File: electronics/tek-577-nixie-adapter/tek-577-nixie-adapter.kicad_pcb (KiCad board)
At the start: 2 copper layers, 31.7 x 61 mm, 3 parts, among them J1 C, J2 B, J3 E

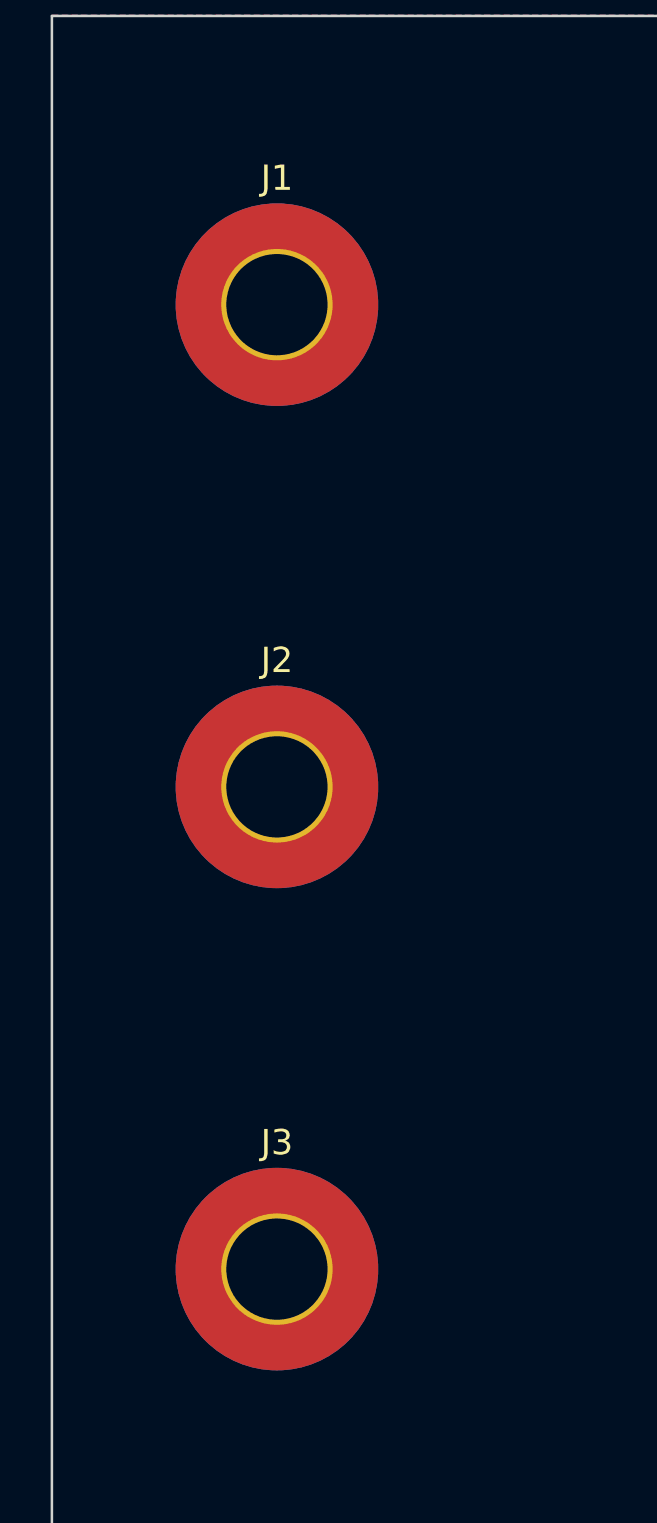
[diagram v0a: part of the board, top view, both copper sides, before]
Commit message: adding symbols
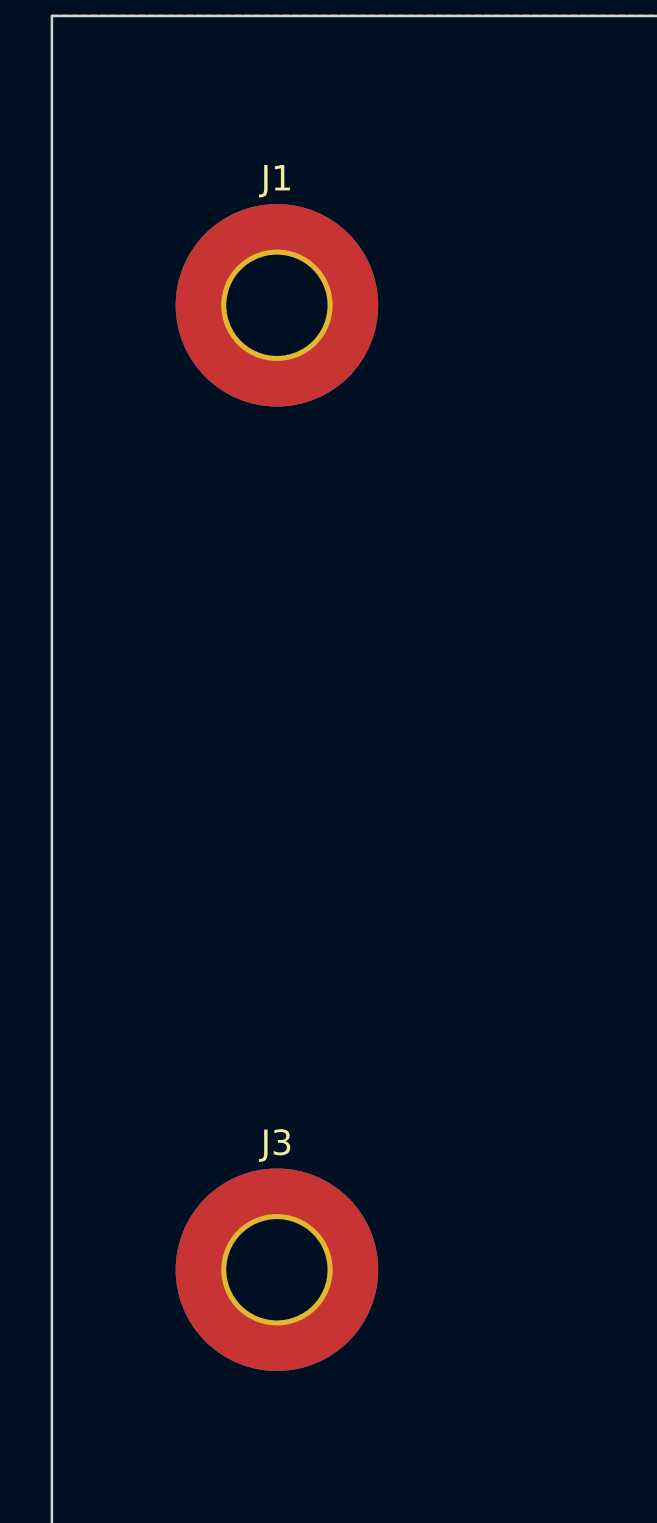
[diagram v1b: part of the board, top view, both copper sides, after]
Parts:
- removed J2: B, MountingHole:MountingHole_4mm_Pad_TopBottom
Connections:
- J1 pad 1: (no net) -> /C
- J3 pad 1: (no net) -> /E
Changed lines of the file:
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@@
   )
   (net 0 "")
+  (net 1 "/C")
+  (net 2 "/E")
   (footprint "MountingHole:MountingHole_4mm_Pad_TopBottom" (layer "F.Cu")
-    (at 134.62 113.005)
+    (at 134.62 74.93)
     (descr "Mounting Hole 4mm")
     (tags "mounting hole 4mm")
-    (property "Sheetfile" "tek-577-fixture-proto.kicad_sch")
+    (property "Sheetfile" "tek-577-nixie-adapter.kicad_sch")
+    (property "Sheetname" "")
+    (property "ki_description" "Generic connector, single row, 01x01, script generated")
+    (property "ki_keywords" "connector")
+    (attr exclude_from_pos_files)
+    (fp_text reference "J1" (at 0 -5) (layer "F.SilkS")
+        (effects (font (size 1 1) (thickness 0.15)))
+    )
+    (fp_text value "C" (at 0 5) (layer "F.Fab")
+        (effects (font (size 1 1) (thickness 0.15)))
+    )
+    (fp_text user "${REFERENCE}" (at 0 0) (layer "F.Fab")
+        (effects (font (size 1 1) (thickness 0.15)))
+    )
+    (fp_circle (center 0 0) (end 4 0)
+      (stroke (width 0.15) (type solid)) (fill none) (layer "Cmts.User"))
+    (fp_circle (center 0 0) (end 4.25 0)
+      (stroke (width 0.05) (type solid)) (fill none) (layer "F.CrtYd"))
+    (pad "1" thru_hole circle (at 0 0) (size 4.4 4.4) (drill 4) (layers "*.Cu" "*.Mask")
+      (net 1 "/C") (pinfunction "Pin_1") (pintype "passive"))
+    (pad "1" connect circle (at 0 0) (size 8 8) (layers "F.Cu" "F.Mask")
+      (net 1 "/C") (pinfunction "Pin_1") (pintype "passive"))
+    (pad "1" connect circle (at 0 0) (size 8 8) (layers "B.Cu" "B.Mask")
+      (net 1 "/C") (pinfunction "Pin_1") (pintype "passive"))
+  )
+  (footprint "MountingHole:MountingHole_4mm_Pad_TopBottom" (layer "F.Cu")
+    (at 134.62 113.03)
+    (descr "Mounting Hole 4mm")
+    (tags "mounting hole 4mm")
+    (property "Sheetfile" "tek-577-nixie-adapter.kicad_sch")
     (property "Sheetname" "")
     (property "ki_description" "Generic connector, single row, 01x01, script generated")
@@
       (stroke (width 0.05) (type solid)) (fill none) (layer "F.CrtYd"))
     (pad "1" thru_hole circle (at 0 0) (size 4.4 4.4) (drill 4) (layers "*.Cu" "*.Mask")
-      (pinfunction "Pin_1") (pintype "passive"))
+      (net 2 "/E") (pinfunction "Pin_1") (pintype "passive"))
     (pad "1" connect circle (at 0 0) (size 8 8) (layers "F.Cu" "F.Mask")
-      (pinfunction "Pin_1") (pintype "passive"))
+      (net 2 "/E") (pinfunction "Pin_1") (pintype "passive"))
     (pad "1" connect circle (at 0 0) (size 8 8) (layers "B.Cu" "B.Mask")
-      (pinfunction "Pin_1") (pintype "passive"))
-  )
-  (footprint "MountingHole:MountingHole_4mm_Pad_TopBottom" (layer "F.Cu")
-    (at 134.62 93.955)
-    (descr "Mounting Hole 4mm")
-    (tags "mounting hole 4mm")
-    (property "Sheetfile" "tek-577-fixture-proto.kicad_sch")
-    (property "Sheetname" "")
-    (property "ki_description" "Generic connector, single row, 01x01, script generated")
-    (property "ki_keywords" "connector")
-    (attr exclude_from_pos_files)
-    (fp_text reference "J2" (at 0 -5) (layer "F.SilkS")
-        (effects (font (size 1 1) (thickness 0.15)))
-    )
-    (fp_text value "B" (at 0 5) (layer "F.Fab")
-        (effects (font (size 1 1) (thickness 0.15)))
-    )
-    (fp_text user "${REFERENCE}" (at 0 0) (layer "F.Fab")
-        (effects (font (size 1 1) (thickness 0.15)))
-    )
-    (fp_circle (center 0 0) (end 4 0)
-      (stroke (width 0.15) (type solid)) (fill none) (layer "Cmts.User"))
-    (fp_circle (center 0 0) (end 4.25 0)
-      (stroke (width 0.05) (type solid)) (fill none) (layer "F.CrtYd"))
-    (pad "1" thru_hole circle (at 0 0) (size 4.4 4.4) (drill 4) (layers "*.Cu" "*.Mask")
-      (pinfunction "Pin_1") (pintype "passive"))
-    (pad "1" connect circle (at 0 0) (size 8 8) (layers "F.Cu" "F.Mask")
-      (pinfunction "Pin_1") (pintype "passive"))
-    (pad "1" connect circle (at 0 0) (size 8 8) (layers "B.Cu" "B.Mask")
-      (pinfunction "Pin_1") (pintype "passive"))
-  )
-  (footprint "MountingHole:MountingHole_4mm_Pad_TopBottom" (layer "F.Cu")
-    (at 134.62 74.905)
-    (descr "Mounting Hole 4mm")
-    (tags "mounting hole 4mm")
-    (property "Sheetfile" "tek-577-fixture-proto.kicad_sch")
-    (property "Sheetname" "")
-    (property "ki_description" "Generic connector, single row, 01x01, script generated")
-    (property "ki_keywords" "connector")
-    (attr exclude_from_pos_files)
-    (fp_text reference "J1" (at 0 -5) (layer "F.SilkS")
-        (effects (font (size 1 1) (thickness 0.15)))
-    )
-    (fp_text value "C" (at 0 5) (layer "F.Fab")
-        (effects (font (size 1 1) (thickness 0.15)))
-    )
-    (fp_text user "${REFERENCE}" (at 0 0) (layer "F.Fab")
-        (effects (font (size 1 1) (thickness 0.15)))
-    )
-    (fp_circle (center 0 0) (end 4 0)
-      (stroke (width 0.15) (type solid)) (fill none) (layer "Cmts.User"))
-    (fp_circle (center 0 0) (end 4.25 0)
-      (stroke (width 0.05) (type solid)) (fill none) (layer "F.CrtYd"))
-    (pad "1" thru_hole circle (at 0 0) (size 4.4 4.4) (drill 4) (layers "*.Cu" "*.Mask")
-      (pinfunction "Pin_1") (pintype "passive"))
-    (pad "1" connect circle (at 0 0) (size 8 8) (layers "F.Cu" "F.Mask")
-      (pinfunction "Pin_1") (pintype "passive"))
-    (pad "1" connect circle (at 0 0) (size 8 8) (layers "B.Cu" "B.Mask")
-      (pinfunction "Pin_1") (pintype "passive"))
+      (net 2 "/E") (pinfunction "Pin_1") (pintype "passive"))
   )
   (gr_rect (start 125.73 63.5) (end 157.48 124.46)

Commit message: working footprints
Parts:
- added N1: IN-4, nixie-us:IN-4-DSUB, F.Cu at (145.1, 94.0)
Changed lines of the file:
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@@
   (net 1 "/C")
   (net 2 "/E")
+  (net 3 "unconnected-(N1-Pad1)")
+  (net 4 "unconnected-(N1-Pad5)")
+  (net 5 "unconnected-(N1-Pad3)")
+  (net 6 "unconnected-(N1-Pad2)")
+  (net 7 "unconnected-(N1-Pad0)")
+  (net 8 "unconnected-(N1-Pad7)")
+  (net 9 "unconnected-(N1-Pad9)")
+  (net 10 "unconnected-(N1-Pad4)")
+  (net 11 "unconnected-(N1-Pad6)")
+  (net 12 "unconnected-(N1-Pad8)")
+  (net 13 "unconnected-(N1-A-PadA3)")
   (footprint "MountingHole:MountingHole_4mm_Pad_TopBottom" (layer "F.Cu")
     (at 134.62 74.93)
@@
       (net 1 "/C") (pinfunction "Pin_1") (pintype "passive"))
   )
+  (footprint "nixie-us:IN-4-DSUB" (layer "F.Cu")
+    (at 145.066716 93.968457)
+    (descr "May be used with socket: <b>PL31-P</b>")
+    (property "Sheetfile" "tek-577-nixie-adapter.kicad_sch")
+    (property "Sheetname" "")
+    (fp_text reference "N1" (at 16.51 0) (layer "F.SilkS")
+        (effects (font (size 1.63576 1.63576) (thickness 0.14224)) (justify left bottom))
+    )
+    (fp_text value "IN-4" (at 0 12.7) (layer "F.SilkS")
+        (effects (font (size 1.63576 1.63576) (thickness 0.14224)))
+    )
+    (fp_text user "TOP" (at 0 -12.7) (layer "F.SilkS")
+        (effects (font (size 1.63576 1.63576) (thickness 0.14224)))
+    )
+    (fp_circle (center -0.033137 0.0873) (end 15.785363 0.0873)
+      (stroke (width 0.254) (type solid)) (fill none) (layer "F.SilkS"))
+    (fp_circle (center 0 0) (end 15.7555 0)
+      (stroke (width 0.254) (type solid)) (fill none) (layer "F.SilkS"))
+    (fp_circle (center 0 0) (end 1.27 0)
+      (stroke (width 2.54) (type solid)) (fill none) (layer "B.Mask"))
+    (fp_circle (center 0 0) (end 1.27 0)
+      (stroke (width 2.54) (type solid)) (fill none) (layer "F.Mask"))
+    (fp_circle (center 0 0) (end 2.54 0)
+      (stroke (width 0.0254) (type solid)) (fill none) (layer "F.Mask"))
+    (pad "" np_thru_hole circle (at -0.033137 0.0873) (size 5 5) (drill 5) (layers "*.Cu" "*.Mask"))
+    (pad "0" thru_hole circle (at -3.793081 -8.083546) (size 2.4 2.4) (drill 1.6) (layers "*.Cu" "*.Mask")
+      (net 7 "unconnected-(N1-Pad0)") (pinfunction "0") (pintype "bidirectional") (solder_mask_margin 0.1016))
+    (pad "1" thru_hole circle (at -1.363328 9.026568) (size 2.4 2.4) (drill 1.6) (layers "*.Cu" "*.Mask")
+      (net 3 "unconnected-(N1-Pad1)") (pinfunction "1") (pintype "bidirectional") (solder_mask_margin 0.1016))
+    (pad "2" thru_hole circle (at -6.783634 -5.848243) (size 2.4 2.4) (drill 1.6) (layers "*.Cu" "*.Mask")
+      (net 6 "unconnected-(N1-Pad2)") (pinfunction "2") (pintype "bidirectional") (solder_mask_margin 0.1016))
+    (pad "3" thru_hole circle (at -8.938068 1.353031) (size 2.4 2.4) (drill 1.6) (layers "*.Cu" "*.Mask")
+      (net 5 "unconnected-(N1-Pad3)") (pinfunction "3") (pintype "bidirectional") (solder_mask_margin 0.1016))
+    (pad "4" thru_hole circle (at 4.793284 7.631543) (size 2.4 2.4) (drill 1.6) (layers "*.Cu" "*.Mask")
+      (net 10 "unconnected-(N1-Pad4)") (pinfunction "4") (pintype "bidirectional") (solder_mask_margin 0.1016))
+    (pad "5" thru_hole circle (at -7.577378 4.913718) (size 2.4 2.4) (drill 1.6) (layers "*.Cu" "*.Mask")
+      (net 4 "unconnected-(N1-Pad5)") (pinfunction "5") (pintype "bidirectional") (solder_mask_margin 0.1016))
+    (pad "6" thru_hole circle (at 7.546737 4.944818) (size 2.4 2.4) (drill 1.6) (layers "*.Cu" "*.Mask")
+      (net 11 "unconnected-(N1-Pad6)") (pinfunction "6") (pintype "bidirectional") (solder_mask_margin 0.1016))
+    (pad "7" thru_hole circle (at 3.70689 -8.101846) (size 2.4 2.4) (drill 1.6) (layers "*.Cu" "*.Mask")
+      (net 8 "unconnected-(N1-Pad7)") (pinfunction "7") (pintype "bidirectional") (solder_mask_margin 0.1016))
+    (pad "8" thru_hole circle (at 8.8779 1.321559) (size 2.4 2.4) (drill 1.6) (layers "*.Cu" "*.Mask")
+      (net 12 "unconnected-(N1-Pad8)") (pinfunction "8") (pintype "bidirectional") (solder_mask_margin 0.1016))
+    (pad "9" thru_hole circle (at 6.788575 -5.777359) (size 2.4 2.4) (drill 1.6) (layers "*.Cu" "*.Mask")
+      (net 9 "unconnected-(N1-Pad9)") (pinfunction "9") (pintype "bidirectional") (solder_mask_margin 0.1016))
+    (pad "A1" thru_hole circle (at -4.918887 7.571237) (size 2.4 2.4) (drill 1.6) (layers "*.Cu" "*.Mask")
+      (solder_mask_margin 0.1016))
+    (pad "A2" thru_hole circle (at -8.70739 -2.46754) (size 2.4 2.4) (drill 1.6) (layers "*.Cu" "*.Mask")
+      (solder_mask_margin 0.1016))
+    (pad "A3" thru_hole circle (at 8.600687 -2.453775) (size 2.4 2.4) (drill 1.6) (layers "*.Cu" "*.Mask")
+      (net 13 "unconnected-(N1-A-PadA3)") (pinfunction "A") (pintype "bidirectional") (solder_mask_margin 0.1016))
+    (pad "N/C" thru_hole circle (at -0.062987 -8.86865) (size 2.4 2.4) (drill 1.6) (layers "*.Cu" "*.Mask")
+      (solder_mask_margin 0.1016))
+  )
   (footprint "MountingHole:MountingHole_4mm_Pad_TopBottom" (layer "F.Cu")

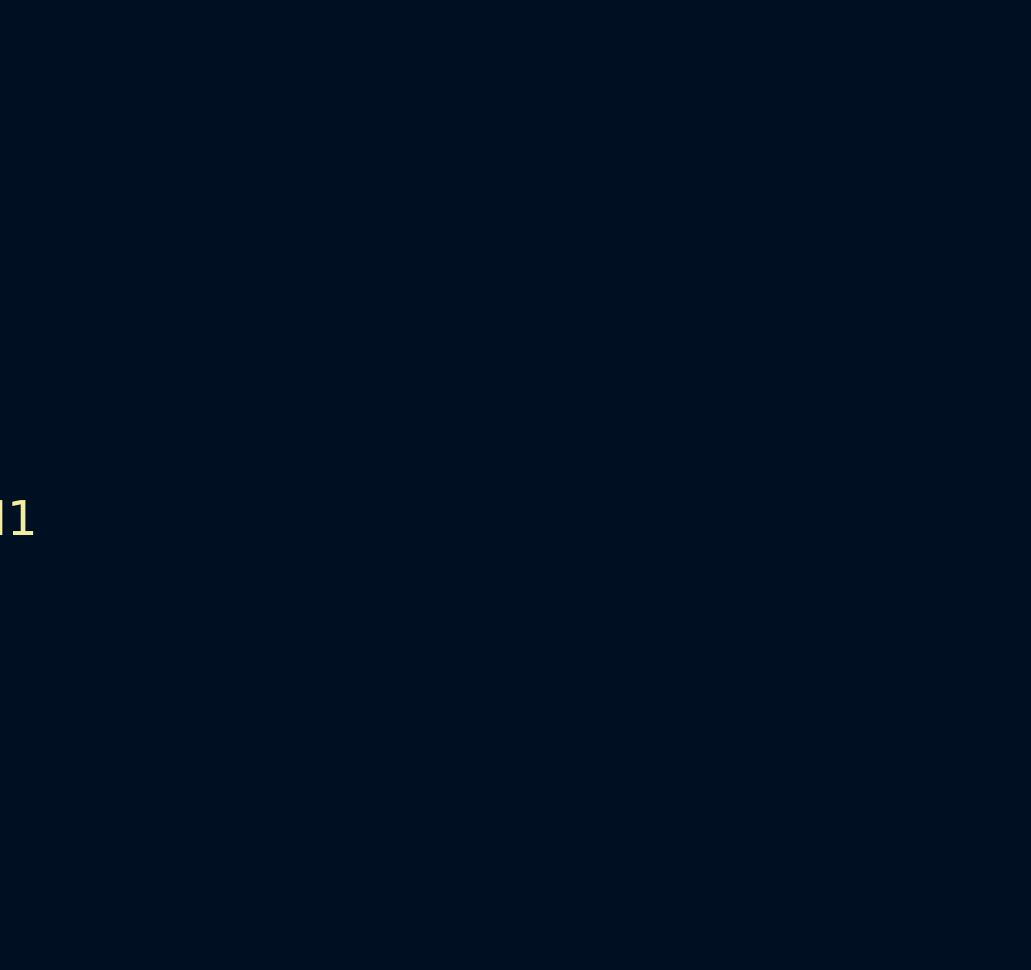
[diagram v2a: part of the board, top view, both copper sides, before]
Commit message: adding the footprints, which only loaded on mac for some reason
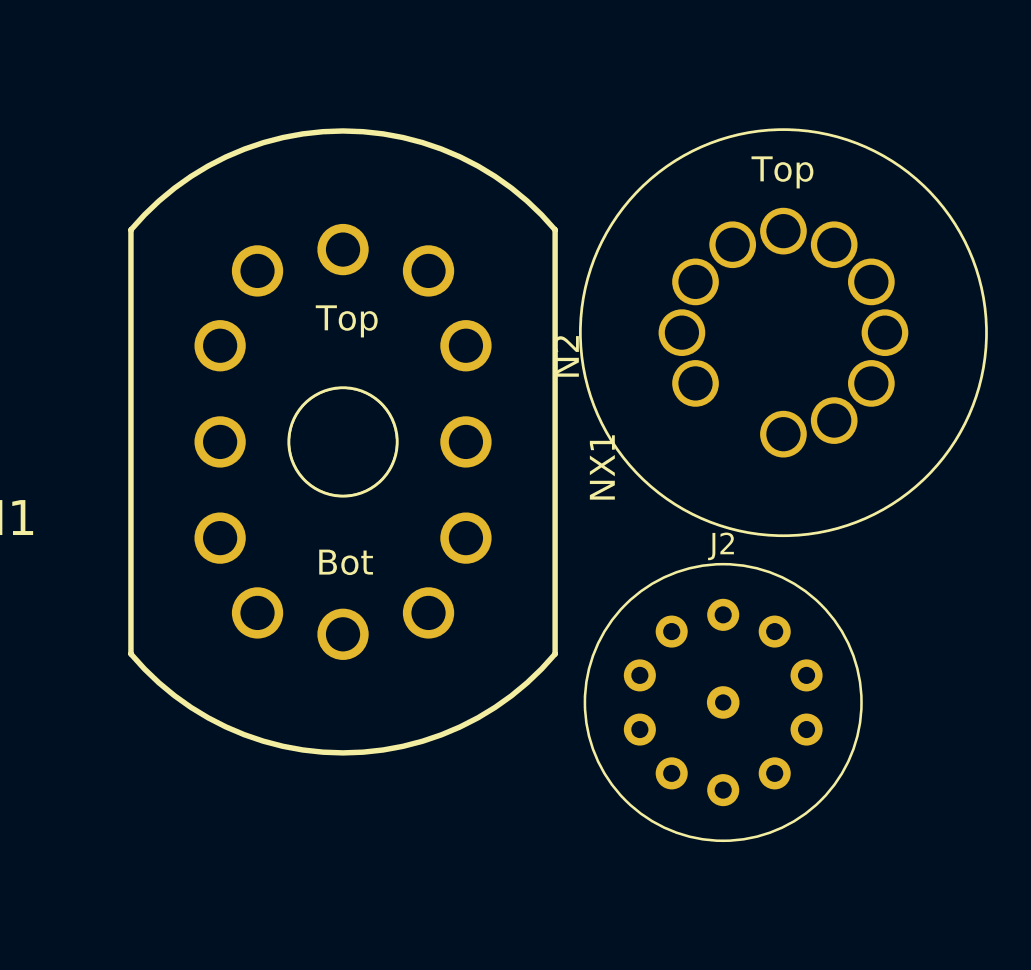
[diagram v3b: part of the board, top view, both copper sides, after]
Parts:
- added J2: Conn_01x11_Socket, Grayhill-Switch:Grayhill Single Pole 10 Position Switch, F.Cu at (196.8, 101.6)
- added N2: IN-2, nixie-us:IN-2-DSUB, F.Cu at (199.6, 84.3)
- added NX1: IN-12BIN-12-DSUB, nixie-us:IN-12-DSUB, F.Cu at (179.0, 89.4)
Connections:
- N1 pad 0: unconnected-(N1-Pad0) -> /0
- N1 pad 1: unconnected-(N1-Pad1) -> /1
- N1 pad 2: unconnected-(N1-Pad2) -> /2
- N1 pad 3: unconnected-(N1-Pad3) -> /3
- N1 pad 4: unconnected-(N1-Pad4) -> /4
- N1 pad 5: unconnected-(N1-Pad5) -> /5
- N1 pad 6: unconnected-(N1-Pad6) -> /6
- N1 pad 7: unconnected-(N1-Pad7) -> /7
- N1 pad 8: unconnected-(N1-Pad8) -> /8
- N1 pad 9: unconnected-(N1-Pad9) -> /9
- N1 pad A3: unconnected-(N1-A-PadA3) -> /C

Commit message: board design done
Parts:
- moved J2 62.6 mm to (134.6, 94.0)
- moved N2 41.7 mm to (159.0, 94.0)
- moved N1 14.0 mm to (159.0, 94.0)
- moved NX1 10.1 mm to (188.0, 94.0)
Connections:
- NX1 pad LHDP: unconnected-(NX1-PadLHDP) -> /E
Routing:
- net /5: track 0.00 -> 122.0 mm, vias 0 -> 3
- net /6: track 0.00 -> 120.9 mm, vias 0 -> 2
- net /8: track 0.00 -> 117.7 mm, vias 0 -> 3
- net /9: track 0.00 -> 110.8 mm, vias 0 -> 2
- net /0: track 0.00 -> 104.0 mm, vias 0 -> 2
- net /7: track 0.00 -> 102.5 mm, vias 0 -> 2
- net /2: track 0.00 -> 101.4 mm, vias 0 -> 3
- net /4: track 0.00 -> 101.0 mm, vias 0 -> 2
- net /3: track 0.00 -> 100.8 mm, vias 0 -> 3
- net /C: track 0.00 -> 99.9 mm, vias 0 -> 2
- net /E: track 0.00 -> 88.7 mm, vias 0 -> 1
- net /1: track 0.00 -> 84.9 mm, vias 0 -> 2
- removed copper zone on B.Cu, net (none)
- removed copper zone on F.Cu, net (none)
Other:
- board size 31.7 x 61 mm -> 76.8 x 61 mm
- board text added: "C"
- board text added: "DECIMAL SHORT"
- board text added: "E"
- board text added: "IN-12B"
- board text added: "IN-2"
- board text added: "TEKTRONIX 577 NIXIE TUBE TEST FIXTURE IN-2 IN-4 IN-12B"
